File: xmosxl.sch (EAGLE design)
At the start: 139 parts, among them IC1 74LVC1T45W6-7, IC2 74LVC1T45W6-7, IC3 74LVC1T45W6-7, IC4 74LVC1T45W6-7, IC5 74LVC1T45W6-7, IC6 74ALVC164245DGG_11, IC7 74ALVC164245DGG_11, IC8 74LVC1T45W6-7, IC9 74LVC1T45W6-7, U1 24 MHz Osc. (F535L-24)

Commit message: Dd the link resistors
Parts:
- added R31, R32, R33, R34, R35: 33R, rcl:R-EU_R0201
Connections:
- new net N$27: R31.1, XMOS-LINK.X1D66@N2
- new net N$28: R32.1, XMOS-LINK.X1D67@P2
- new net N$29: R34.1, XMOS-LINK.X1D69@R1
- new net N$30: R35.1, XMOS-LINK.X1D70@R2
- net +5V: no longer JP1.13
- net RX0: no longer JP1.5
- net RX1: now also JP1.5; no longer JP1.9
- net RX2: now also JP1.9
- net RX3: now also JP1.13
- net RX4: now also R33.1
- net TX0: now also R31.2
- net TX1: now also R32.2
- net TX2: now also R33.2
- net TX3: now also R34.2
- net TX4: now also R35.2
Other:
- note removed: "Need to fix the RX lines, add 33R to tx, and place on grid"
- moved on the sheet: JP1

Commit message: Board circuit-complete. Decided to ditch the SPI expansion.
Need to set signal classes and routing hints
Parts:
- added JP2: (no value), pinhead:PINHD-2X9
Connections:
- new net XPND_CTRL0: JP2.3, XMOS-EXPAND.X3D00@D19
- new net XPND_CTRL1: JP2.5, XMOS-EXPAND.X3D01@D20
- new net XPND_CTRL2: JP2.7, XMOS-EXPAND.X3D10@C13
- new net XPND_CTRL3: JP2.9, XMOS-EXPAND.X3D11@D13
- new net XPND_CTRL4: JP2.11, XMOS-EXPAND.X3D12@AA12
- new net XPND_CTRL5: JP2.13, XMOS-EXPAND.X3D13@Y15
- new net XPND_CTRL6: JP2.15, XMOS-EXPAND.X3D24@Y19
- new net XPND_DATA0: JP2.2, XMOS-EXPAND.X3D02@U21
- new net XPND_DATA1: JP2.4, XMOS-EXPAND.X3D03@T21
- new net XPND_DATA2: JP2.6, XMOS-EXPAND.X3D04@R20
- new net XPND_DATA3: JP2.8, XMOS-EXPAND.X3D05@R21
- new net XPND_DATA4: JP2.10, XMOS-EXPAND.X3D06@P20
- new net XPND_DATA5: JP2.12, XMOS-EXPAND.X3D07@P21
- new net XPND_DATA6: JP2.14, XMOS-EXPAND.X3D08@E20
- new net XPND_DATA7: JP2.16, XMOS-EXPAND.X3D09@E21
- net +3V3: now also SLOT1.B16, SLOT2.B17, SLOT3.B16, SLOT3.B17, SLOT4.B18, SLOT5.B16, SLOT5.B18; no longer JP1.11, JP1.12
- net +5V: now also JP1.3, JP1.4, JP2.1, SLOT1.A1, SLOT1.A2, SLOT1.B1, SLOT1.B2, SLOT2.A1, SLOT2.A2, SLOT2.B1, SLOT2.B2, SLOT3.A1, SLOT3.A2, SLOT3.B1, SLOT3.B2, SLOT4.A1, SLOT4.A2, SLOT4.B1, SLOT4.B2, SLOT5.A1, SLOT5.A2, SLOT5.B1, SLOT5.B2
- net GND: now also JP1.11, JP1.12, JP1.15, JP1.16, JP2.17, JP2.18, SLOT1.B17, SLOT1.B18, SLOT1.B19, SLOT1.B20, SLOT1.B21, SLOT1.B22, SLOT1.B23, SLOT1.B24, SLOT1.B25, SLOT1.B26, SLOT1.B27, SLOT1.B28, SLOT1.B29, SLOT1.B30, SLOT1.B31, SLOT1.B32, SLOT2.B16, SLOT2.B18, SLOT2.B19, SLOT2.B20, SLOT2.B21, SLOT2.B22, SLOT2.B23, SLOT2.B24, SLOT2.B25, SLOT2.B26, SLOT2.B27, SLOT2.B28, SLOT2.B29, SLOT2.B30, SLOT2.B31, SLOT2.B32, SLOT3.B18, SLOT3.B19, SLOT3.B20, SLOT3.B21, SLOT3.B22, SLOT3.B23, SLOT3.B24, SLOT3.B25, SLOT3.B26, SLOT3.B27, SLOT3.B28, SLOT3.B29, SLOT3.B30, SLOT3.B31, SLOT3.B32, SLOT4.B16, SLOT4.B17, SLOT4.B19, SLOT4.B20, SLOT4.B21, SLOT4.B22, SLOT4.B23, SLOT4.B24, SLOT4.B25, SLOT4.B26, SLOT4.B27, SLOT4.B28, SLOT4.B29, SLOT4.B30, SLOT4.B31, SLOT4.B32, SLOT5.B17, SLOT5.B19, SLOT5.B20, SLOT5.B21, SLOT5.B22, SLOT5.B23, SLOT5.B24, SLOT5.B25, SLOT5.B26, SLOT5.B27, SLOT5.B28, SLOT5.B29, SLOT5.B30, SLOT5.B31, SLOT5.B32; no longer JP1.3, JP1.4
- net SBUS_A0: now also SLOT1.A3, SLOT2.A3, SLOT3.A3, SLOT4.A3, SLOT5.A3
- net SBUS_A1: now also SLOT1.A4, SLOT2.A4, SLOT3.A4, SLOT4.A4, SLOT5.A4
- net SBUS_A10: now also SLOT1.A13, SLOT2.A13, SLOT3.A13, SLOT4.A13, SLOT5.A13
- net SBUS_A11: now also SLOT1.A14, SLOT2.A14, SLOT3.A14, SLOT4.A14, SLOT5.A14
- net SBUS_A12: now also SLOT1.A15, SLOT2.A15, SLOT3.A15, SLOT4.A15, SLOT5.A15
- net SBUS_A13: now also SLOT1.A16, SLOT2.A16, SLOT3.A16, SLOT4.A16, SLOT5.A16
- net SBUS_A14: now also SLOT1.A17, SLOT2.A17, SLOT3.A17, SLOT4.A17, SLOT5.A17
- net SBUS_A15: now also SLOT1.A18, SLOT2.A18, SLOT3.A18, SLOT4.A18, SLOT5.A18
- net SBUS_A2: now also SLOT1.A5, SLOT2.A5, SLOT3.A5, SLOT4.A5, SLOT5.A5
- net SBUS_A3: now also SLOT1.A6, SLOT2.A6, SLOT3.A6, SLOT4.A6, SLOT5.A6
- net SBUS_A4: now also SLOT1.A7, SLOT2.A7, SLOT3.A7, SLOT4.A7, SLOT5.A7
- net SBUS_A5: now also SLOT1.A8, SLOT2.A8, SLOT3.A8, SLOT4.A8, SLOT5.A8
- net SBUS_A6: now also SLOT1.A9, SLOT2.A9, SLOT3.A9, SLOT4.A9, SLOT5.A9
- net SBUS_A7: now also SLOT1.A10, SLOT2.A10, SLOT3.A10, SLOT4.A10, SLOT5.A10
- net SBUS_A8: now also SLOT1.A11, SLOT2.A11, SLOT3.A11, SLOT4.A11, SLOT5.A11
- net SBUS_A9: now also SLOT1.A12, SLOT2.A12, SLOT3.A12, SLOT4.A12, SLOT5.A12
- net SBUS_CLK: now also SLOT1.A19, SLOT2.A19, SLOT3.A19, SLOT4.A19, SLOT5.A19
- net SBUS_D0: now also SLOT1.A20, SLOT2.A20, SLOT3.A20, SLOT4.A20, SLOT5.A20
- net SBUS_D1: now also SLOT1.A21, SLOT2.A21, SLOT3.A21, SLOT4.A21, SLOT5.A21
- net SBUS_D2: now also SLOT1.A22, SLOT2.A22, SLOT3.A22, SLOT4.A22, SLOT5.A22
- net SBUS_D3: now also SLOT1.A23, SLOT2.A23, SLOT3.A23, SLOT4.A23, SLOT5.A23
- net SBUS_D4: now also SLOT1.A24, SLOT2.A24, SLOT3.A24, SLOT4.A24, SLOT5.A24
- net SBUS_D5: now also SLOT1.A25, SLOT2.A25, SLOT3.A25, SLOT4.A25, SLOT5.A25
- net SBUS_D6: now also SLOT1.A26, SLOT2.A26, SLOT3.A26, SLOT4.A26, SLOT5.A26
- net SBUS_D7: now also SLOT1.A27, SLOT2.A27, SLOT3.A27, SLOT4.A27, SLOT5.A27
- net SBUS_FLG0: now also SLOT1.A28, SLOT2.A28, SLOT3.A28, SLOT4.A28, SLOT5.A28
- net SBUS_FLG1: now also SLOT1.A29, SLOT2.A29, SLOT3.A29, SLOT4.A29, SLOT5.A29
- net SBUS_FLG2: now also SLOT1.A30, SLOT2.A30, SLOT3.A30, SLOT4.A30, SLOT5.A30
- net SBUS_FLG3: now also SLOT1.A31, SLOT2.A31, SLOT3.A31, SLOT4.A31, SLOT5.A31
- net SBUS_FLG4: now also SLOT1.A32, SLOT2.A32, SLOT3.A32, SLOT4.A32, SLOT5.A32
- net SPI_BOPT0: now also SLOT1.B3, SLOT2.B3, SLOT3.B3, SLOT4.B3, SLOT5.B3
- net SPI_BOPT1: now also SLOT1.B4, SLOT2.B4, SLOT3.B4, SLOT4.B4, SLOT5.B4
- net SPI_BOPT2: now also SLOT1.B5, SLOT2.B5, SLOT3.B5, SLOT4.B5, SLOT5.B5
- net SPI_BOPT3: now also SLOT1.B6, SLOT2.B6, SLOT3.B6, SLOT4.B6, SLOT5.B6
- net SPI_BSEL0: now also SLOT1.B7, SLOT2.B7, SLOT3.B7, SLOT4.B7, SLOT5.B7
- net SPI_BSEL1: now also SLOT1.B8, SLOT2.B8, SLOT3.B8, SLOT4.B8, SLOT5.B8
- net SPI_BSEL2: now also SLOT1.B9, SLOT2.B9, SLOT3.B9, SLOT4.B9, SLOT5.B9
- net SPI_BSEL3: now also SLOT1.B10, SLOT2.B10, SLOT3.B10, SLOT4.B10, SLOT5.B10
- net SPI_CLK0: now also SLOT1.B11, SLOT2.B11, SLOT3.B11, SLOT4.B11, SLOT5.B11
- net SPI_IRQ0: now also SLOT1.B12
- net SPI_IRQ1: now also SLOT2.B12
- net SPI_IRQ2: now also SLOT3.B12
- net SPI_IRQ3: now also SLOT4.B12
- net SPI_IRQ4: now also SLOT5.B12
- net SPI_MISO0: now also SLOT1.B13, SLOT2.B13, SLOT3.B13, SLOT4.B13, SLOT5.B13
- net SPI_MOSI0: now also SLOT1.B14, SLOT2.B14, SLOT3.B14, SLOT4.B14, SLOT5.B14
- net SPI_SS0: now also SLOT1.B15
- net SPI_SS1: now also SLOT2.B15
- net SPI_SS2: now also SLOT3.B15
- net SPI_SS3: now also SLOT4.B15
- net SPI_SS4: now also SLOT5.B15
- net VDD: no longer JP1.15, JP1.16
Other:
- moved on the sheet: SLOT1, SLOT2, SLOT3

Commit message: Start reconfiguring for STM
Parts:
- removed C10, C11, C14, C21, C22, C23, C24, C25, C26, C27, C28, C29, C30, C31, C32, C33, C34, C35, C36, C37, C38, C39, C4, C40, C43, C54, C55, C58, C7, C8, C9: 0.1uF, rcl:C-EUC0201
- removed C41, C42, C47: 10uF, rcl:C-EUC0402K
- removed C46, C48: 1uF, rcl:C-EUC0402K
- removed C49: 0.1uF, rcl:C-EUC0402
- removed C50: 120pF, rcl:C-EUC0402
- removed C56: 120pF, rcl:C-EUC0201
- removed C57: 10nF, rcl:C-EUC0201
- removed C59, C60, C61, C62, C63, C64, C65, C66: 100nF, rcl:C-EUC0201
- removed I2C0, I2C1: (no value), pinhead:PINHD-1X2
- removed IC2, IC3, IC4, IC5: 74LVC1T45W6-7, samacsys:74LVC1T45W6-7
- removed JP2: (no value), pinhead:PINHD-2X9
- removed JTAG5V: PSU, pinhead:PINHD-1X2
- removed NOR: SN74LVC1G02, sjg-logic:SN74LVC1G02
- removed R1, R12, R13, R18, R19, R2, R22, R23, R25, R26, R3, R5, R6, R7, R9: 10K, rcl:R-EU_R0201
- removed R10: 47K, rcl:R-EU_R0402
- removed R14, R15: 47K, rcl:R-EU_R0201
- removed R16, R17, R31, R32, R33, R34, R35: 33R, rcl:R-EU_R0201
- removed R24: 2.2R, rcl:R-EU_R0201
- removed R27, R28: 43R2, rcl:R-EU_R0201
- removed R29, R30: 4K7, rcl:R-EU_R0201
- removed RESET_SW: MANUAL_RESET, SparkFun:TAC_SWITCHPTH
- removed U$11: TPS3808G09DBVR, sjg-power:TPS3808G09DBVR
- removed U$3: LD49300, sjg-power:LD49150
- removed U$4: TPS3808G33DBVR, sjg-power:TPS3808DBVR
- removed U$5: 74LVC1G07SE-7, sjg-logic:74LVC1G07SE-7
- removed U$7: W9852G6KH, sjg-sdram:W9852G6KH
- removed UART: (no value), pinhead:PINHD-1X3
- removed XMOS: XEF232, xmosxl:XEF232
- removed XTAG: 1175-1618-ND, pinhead:PINHD-2X10/90
- added SLOT6: PCIE_64, pcie:PCIE_64
- added U$1: STM32F767, xmosxl:STM32F767
- C1, C2: value 0.1uF -> 10uF; device rcl:C-EUC0201 -> rcl:C-EUC0402K; USE GRM033C80J104ME15D -> (none)
- C3: value 0.1uF -> 1uF
- IC1: value 74LVC1T45W6-7 -> MCP1727-1802E_SN; device samacsys:74LVC1T45W6-7 -> samacsys:MCP1727-1802E_SN
- JP1: device pinhead:PINHD-2X9 -> pinhead:PINHD-2X20
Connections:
- removed net !DEBUG!: XMOS-CTRL.!DEBUG!@D9, XTAG.11
- removed net !HALT!_DIR: IC4.DIR, R7.1, XMOS-A8BUS.X3D29@C14
- removed net !IRQ!: IC3.B, XMOS-A8BUS.X2D35@B21
- removed net !IRQ!_DIR: IC3.DIR, R6.1, XMOS-A8BUS.X3D28@D14
- removed net !REF!_DIR: IC8.DIR, R9.1, XMOS-A8BUS.X3D30@A15
- removed net !RESET!: R15.1, U$11.!RESET!@1, U$5.Y@4, XMOS-CTRL.!RST!@B12, XMOS-CTRL.!TRST!@C12
- removed net !RST!_DIR: IC2.DIR, R5.1, XMOS-A8BUS.X3D27@B16
- removed net !SD_CAS!: NORG$1.I0, U$7.!CAS!@17, XMOS-SDRAM.X2D20@Y18
- removed net !SD_RAS!: U$7.!RAS!@18, XMOS-SDRAM.X2D02@Y13
- removed net !SD_WE!: NORG$1.I1, U$7.!WE!@16, XMOS-SDRAM.X2D21@AA18
- removed net A_DIR: IC7.1DIR, IC7.2DIR, R2.1, XMOS-A8BUS.X3D31@B15
- removed net D_DIR: IC6.1DIR, R3.1, XMOS-A8BUS.X3D32@A14
- removed net EN_1V0: R10.1, U$3.EN, U$4.!RESET!@1
- removed net JTAG_DN0: XMOS-LINK.X1D17@U1, XTAG.14
- removed net JTAG_DN1: XMOS-LINK.X1D16@U2, XTAG.18
- removed net JTAG_UP0: R16.2, XTAG.10
- removed net JTAG_UP1: R17.2, XTAG.6
- removed net N$1: R14.1, U$5.A@2, XTAG.15
- removed net N$10: R26.2, XMOS-CTRL.MODE0@D10
- removed net N$11: R27.2, XMOS-USB.USB_RTUNE_1@W16
- removed net N$12: R28.2, XMOS-USB.USB_RTUNE_0@W6
- removed net N$13: UART.2, XMOS-UART.X1D35@E3
- removed net N$14: NORG$1.O, U$7.LDQM@15, U$7.UDQM@39
- removed net N$15: R12.2, U$7.CKE@37
- removed net N$17: R13.2, U$7.!CS!@19
- removed net N$20: UART.1, XMOS-UART.X1D34@D3
- removed net N$22: R16.1, XMOS-LINK.X1D18@V2
- removed net N$23: R17.1, XMOS-LINK.X1D19@V1
- removed net N$27: R31.1, XMOS-LINK.X1D66@N2
- removed net N$28: R32.1, XMOS-LINK.X1D67@P2
- removed net N$29: R34.1, XMOS-LINK.X1D69@R1
- removed net N$30: R35.1, XMOS-LINK.X1D70@R2
- removed net N$38: JTAG5V.2, XTAG.1
- removed net N$5: C50.1, U$4.CT@4
- removed net N$6: C56.1, U$11.CT@4
- removed net N$7: C58.1, R24.2, XMOS-POWER.PLL_AVDD@F11
- removed net N$8: R14.2, U$5.VCC@5
- removed net N$9: R25.1, XMOS-CTRL.MODE1@C10
- removed net R/!W!_DIR: IC1.DIR, R1.1, XMOS-A8BUS.X3D26@D15
- removed net RD4: IC6.2A1, XMOS-A8BUS.X3D20@W18
- removed net RD5: IC6.2A0, XMOS-A8BUS.X3D21@V18
- removed net RX0: JP1.1, XMOS-LINK.X1D65@N1
- removed net RX1: JP1.5, XMOS-LINK.X1D64@M1
- removed net RX2: JP1.9, XMOS-LINK.X1D63@M2
- removed net RX3: JP1.13, XMOS-LINK.X1D62@M3
- removed net RX4: JP1.17, R33.1, XMOS-LINK.X1D61@L3, XMOS-LINK.X1D68@P1
- removed net SBUS_A0: SLOT1.A3, SLOT2.A3, SLOT3.A3, SLOT4.A3, SLOT5.A3, XMOS-SLOTBUS.X1D26@A5
- removed net SBUS_A1: SLOT1.A4, SLOT2.A4, SLOT3.A4, SLOT4.A4, SLOT5.A4, XMOS-SLOTBUS.X1D27@B5
- removed net SBUS_A10: SLOT1.A13, SLOT2.A13, SLOT3.A13, SLOT4.A13, SLOT5.A13, XMOS-SLOTBUS.X1D38@T1
- removed net SBUS_A11: SLOT1.A14, SLOT2.A14, SLOT3.A14, SLOT4.A14, SLOT5.A14, XMOS-SLOTBUS.X1D39@U3
- removed net SBUS_A12: SLOT1.A15, SLOT2.A15, SLOT3.A15, SLOT4.A15, SLOT5.A15, XMOS-SLOTBUS.X1D40@B7
- removed net SBUS_A13: SLOT1.A16, SLOT2.A16, SLOT3.A16, SLOT4.A16, SLOT5.A16, XMOS-SLOTBUS.X1D41@A7
- removed net SBUS_A14: SLOT1.A17, SLOT2.A17, SLOT3.A17, SLOT4.A17, SLOT5.A17, XMOS-SLOTBUS.X1D42@B6
- removed net SBUS_A15: SLOT1.A18, SLOT2.A18, SLOT3.A18, SLOT4.A18, SLOT5.A18, XMOS-SLOTBUS.X1D43@C6
- removed net SBUS_A2: SLOT1.A5, SLOT2.A5, SLOT3.A5, SLOT4.A5, SLOT5.A5, XMOS-SLOTBUS.X1D28@C5
- removed net SBUS_A3: SLOT1.A6, SLOT2.A6, SLOT3.A6, SLOT4.A6, SLOT5.A6, XMOS-SLOTBUS.X1D29@D5
- removed net SBUS_A4: SLOT1.A7, SLOT2.A7, SLOT3.A7, SLOT4.A7, SLOT5.A7, XMOS-SLOTBUS.X1D30@C4
- removed net SBUS_A5: SLOT1.A8, SLOT2.A8, SLOT3.A8, SLOT4.A8, SLOT5.A8, XMOS-SLOTBUS.X1D31@D4
- removed net SBUS_A6: SLOT1.A9, SLOT2.A9, SLOT3.A9, SLOT4.A9, SLOT5.A9, XMOS-SLOTBUS.X1D32@A4
- removed net SBUS_A7: SLOT1.A10, SLOT2.A10, SLOT3.A10, SLOT4.A10, SLOT5.A10, XMOS-SLOTBUS.X1D33@B4
- removed net SBUS_A8: SLOT1.A11, SLOT2.A11, SLOT3.A11, SLOT4.A11, SLOT5.A11, XMOS-SLOTBUS.X1D36@F1
- removed net SBUS_A9: SLOT1.A12, SLOT2.A12, SLOT3.A12, SLOT4.A12, SLOT5.A12, XMOS-SLOTBUS.X1D37@R3
- removed net SBUS_CLK: SLOT1.A19, SLOT2.A19, SLOT3.A19, SLOT4.A19, SLOT5.A19, XMOS-SLOTBUS.X1D21@AA8
- removed net SBUS_D0: SLOT1.A20, SLOT2.A20, SLOT3.A20, SLOT4.A20, SLOT5.A20, XMOS-SLOTBUS.X1D49@G1
- removed net SBUS_D1: SLOT1.A21, SLOT2.A21, SLOT3.A21, SLOT4.A21, SLOT5.A21, XMOS-SLOTBUS.X1D50@G2
- removed net SBUS_D2: SLOT1.A22, SLOT2.A22, SLOT3.A22, SLOT4.A22, SLOT5.A22, XMOS-SLOTBUS.X1D51@G3
- removed net SBUS_D3: SLOT1.A23, SLOT2.A23, SLOT3.A23, SLOT4.A23, SLOT5.A23, XMOS-SLOTBUS.X1D52@H2
- removed net SBUS_D4: SLOT1.A24, SLOT2.A24, SLOT3.A24, SLOT4.A24, SLOT5.A24, XMOS-SLOTBUS.X1D53@H1
- removed net SBUS_D5: SLOT1.A25, SLOT2.A25, SLOT3.A25, SLOT4.A25, SLOT5.A25, XMOS-SLOTBUS.X1D54@J1
- removed net SBUS_D6: SLOT1.A26, SLOT2.A26, SLOT3.A26, SLOT4.A26, SLOT5.A26, XMOS-SLOTBUS.X1D55@J2
- removed net SBUS_D7: SLOT1.A27, SLOT2.A27, SLOT3.A27, SLOT4.A27, SLOT5.A27, XMOS-SLOTBUS.X1D56@K3
- removed net SBUS_FLG0: SLOT1.A28, SLOT2.A28, SLOT3.A28, SLOT4.A28, SLOT5.A28, XMOS-SLOTBUS.X1D57@K2
- removed net SBUS_FLG1: SLOT1.A29, SLOT2.A29, SLOT3.A29, SLOT4.A29, SLOT5.A29, XMOS-SLOTBUS.X1D58@K1
- removed net SBUS_FLG2: SLOT1.A30, SLOT2.A30, SLOT3.A30, SLOT4.A30, SLOT5.A30, XMOS-SLOTBUS.X1D14@V8
- removed net SBUS_FLG3: SLOT1.A31, SLOT2.A31, SLOT3.A31, SLOT4.A31, SLOT5.A31, XMOS-SLOTBUS.X1D15@W8
- removed net SBUS_FLG4: SLOT1.A32, SLOT2.A32, SLOT3.A32, SLOT4.A32, SLOT5.A32, XMOS-SLOTBUS.X1D20@Y8
- removed net SCL: I2C0.1, I2C1.1, R29.1, XMOS-I2C.X1D11@A3
- removed net SDA: I2C0.2, I2C1.2, R30.1, XMOS-I2C.X1D10@B3
- removed net SD_ADQ0: U$7.A0@23, U$7.DQ0@2, XMOS-SDRAM.X2D03@AA13
- removed net SD_ADQ1: R19.2, U$7.A1@24, U$7.DQ1@4, XMOS-SDRAM.X2D04@W13
- removed net SD_ADQ10: U$7.A10/AP@22, U$7.DQ10@45, XMOS-SDRAM.X2D14@Y17
- removed net SD_ADQ11: U$7.A11@35, U$7.DQ11@47, XMOS-SDRAM.X2D15@AA17
- removed net SD_ADQ12: U$7.A12@36, U$7.DQ12@48, XMOS-SDRAM.X2D16@W21
- removed net SD_ADQ13: U$7.BS0@20, U$7.DQ13@50, XMOS-SDRAM.X2D17@V20
- removed net SD_ADQ14: U$7.BS1@21, U$7.DQ14@51, XMOS-SDRAM.X2D18@V21
- removed net SD_ADQ15: U$7.DQ15@53, XMOS-SDRAM.X2D19@U20
- removed net SD_ADQ2: R22.2, U$7.A2@25, U$7.DQ2@5, XMOS-SDRAM.X2D05@V13
- removed net SD_ADQ3: R18.2, U$7.A3@26, U$7.DQ3@7, XMOS-SDRAM.X2D06@W14
- removed net SD_ADQ4: U$7.A4@29, U$7.DQ4@8, XMOS-SDRAM.X2D07@V14
- removed net SD_ADQ5: U$7.A5@30, U$7.DQ5@10, XMOS-SDRAM.X2D08@Y14
- removed net SD_ADQ6: U$7.A6@31, U$7.DQ6@11, XMOS-SDRAM.X2D09@AA14
- removed net SD_ADQ7: R23.2, U$7.A7@32, U$7.DQ7@13, XMOS-SDRAM.X2D11@Y12
- removed net SD_ADQ8: U$7.A8@33, U$7.DQ8@42, XMOS-SDRAM.X2D12@V19
- removed net SD_ADQ9: U$7.A9@34, U$7.DQ9@44, XMOS-SDRAM.X2D13@Y20
- removed net SD_CLK: U$7.CLK@38, XMOS-SDRAM.X2D00@W12
- removed net SPI_BOPT0: SLOT1.B3, SLOT2.B3, SLOT3.B3, SLOT4.B3, SLOT5.B3, XMOS-SPI.X0D14@W9
- removed net SPI_BOPT1: SLOT1.B4, SLOT2.B4, SLOT3.B4, SLOT4.B4, SLOT5.B4, XMOS-SPI.X0D15@Y9
- removed net SPI_BOPT2: SLOT1.B5, SLOT2.B5, SLOT3.B5, SLOT4.B5, SLOT5.B5, XMOS-SPI.X0D20@AA9
- removed net SPI_BOPT3: SLOT1.B6, SLOT2.B6, SLOT3.B6, SLOT4.B6, SLOT5.B6, XMOS-SPI.X0D21@V10
- removed net SPI_BSEL0: SLOT1.B7, SLOT2.B7, SLOT3.B7, SLOT4.B7, SLOT5.B7, XMOS-SPI.X0D02@V4
- removed net SPI_BSEL1: SLOT1.B8, SLOT2.B8, SLOT3.B8, SLOT4.B8, SLOT5.B8, XMOS-SPI.X0D03@W4
- removed net SPI_BSEL2: SLOT1.B9, SLOT2.B9, SLOT3.B9, SLOT4.B9, SLOT5.B9, XMOS-SPI.X0D08@V5
- removed net SPI_BSEL3: SLOT1.B10, SLOT2.B10, SLOT3.B10, SLOT4.B10, SLOT5.B10, XMOS-SPI.X0D09@W5
- removed net SPI_CLK0: SLOT1.B11, SLOT2.B11, SLOT3.B11, SLOT4.B11, SLOT5.B11, XMOS-SPI.X0D00@Y2
- removed net SPI_CLK1: XMOS-SPI.X1D22@W2
- removed net SPI_IRQ0: SLOT1.B12, XMOS-SPI.X0D28@B9
- removed net SPI_IRQ1: SLOT2.B12, XMOS-SPI.X0D29@A9
- removed net SPI_IRQ2: SLOT3.B12, XMOS-SPI.X0D30@B8
- removed net SPI_IRQ3: SLOT4.B12, XMOS-SPI.X0D31@A8
- removed net SPI_IRQ4: SLOT5.B12, XMOS-SPI.X0D32@C9
- removed net SPI_IRQ5: XMOS-SPI.X0D33@C8
- removed net SPI_IRQ6: XMOS-SPI.X0D40@D2
- removed net SPI_IRQ7: XMOS-SPI.X0D41@D1
- removed net SPI_IRQ8: XMOS-SPI.X0D42@E2
- removed net SPI_IRQ9: XMOS-SPI.X0D43@E1
- removed net SPI_MISO0: SLOT1.B13, SLOT2.B13, SLOT3.B13, SLOT4.B13, SLOT5.B13, XMOS-SPI.X0D11@V6
- removed net SPI_MISO1: XMOS-SPI.X1D23@Y1
- removed net SPI_MOSI0: SLOT1.B14, SLOT2.B14, SLOT3.B14, SLOT4.B14, SLOT5.B14, XMOS-SPI.X0D12@W10
- removed net SPI_MOSI1: XMOS-SPI.X1D24@Y7
- removed net SPI_SS0: SLOT1.B15, XMOS-SPI.X0D13@Y10
- removed net SPI_SS1: SLOT2.B15, XMOS-SPI.X0D22@AA10
- removed net SPI_SS2: SLOT3.B15, XMOS-SPI.X0D23@W11
- removed net SPI_SS3: SLOT4.B15, XMOS-SPI.X0D36@B2
- removed net SPI_SS4: SLOT5.B15, XMOS-SPI.X0D37@B1
- removed net SPI_SS5: XMOS-SPI.X0D38@C2
- removed net SPI_SS6: XMOS-SPI.X0D39@C1
- removed net SPI_SS7: XMOS-SPI.X1D12@Y5
- removed net SPI_SS8: XMOS-SPI.X1D13@AA5
- removed net SPI_SS9: XMOS-SPI.X1D25@V9
- removed net TCK: XMOS-CTRL.TCK@B13, XTAG.9
- removed net TDI: XMOS-CTRL.TDI@A10, XTAG.5
- removed net TDO: XMOS-CTRL.TDO@A13, XTAG.13
- removed net TMS: XMOS-CTRL.TMS@D12, XTAG.7
- removed net TRST_N: C57.2, RESET_SW.1, RESET_SW.2, U$11.!MR!@3
- removed net TX0: JP1.2, R31.2
- removed net TX1: JP1.6, R32.2
- removed net TX2: JP1.10, R33.2
- removed net TX3: JP1.14, R34.2
- removed net TX4: JP1.18, R35.2
- removed net UART_RX: XTAG.19
- removed net UART_TX: XTAG.17
- removed net VDD: C29.1, C30.1, C31.1, C32.1, C33.1, C34.1, C35.1, C36.1, C37.1, C38.1, C39.1, C40.1, C42.1, C47.1, R24.1, U$11.SENSE@5, U$3.VOUT, XMOS-POWER.VDD@C19, XMOS-POWER.VDD@C3, XMOS-POWER.VDD@E13, XMOS-POWER.VDD@E14, XMOS-POWER.VDD@E17, XMOS-POWER.VDD@E18, XMOS-POWER.VDD@E4, XMOS-POWER.VDD@E5, XMOS-POWER.VDD@E8, XMOS-POWER.VDD@E9, XMOS-POWER.VDD@F12, XMOS-POWER.VDD@F13, XMOS-POWER.VDD@F14, XMOS-POWER.VDD@F15, XMOS-POWER.VDD@F16, XMOS-POWER.VDD@F17, XMOS-POWER.VDD@F18, XMOS-POWER.VDD@F4, XMOS-POWER.VDD@F5, XMOS-POWER.VDD@F6, XMOS-POWER.VDD@F7, XMOS-POWER.VDD@F8, XMOS-POWER.VDD@F9, XMOS-POWER.VDD@H19, XMOS-POWER.VDD@H3, XMOS-POWER.VDD@J19, XMOS-POWER.VDD@J3, XMOS-POWER.VDD@N19, XMOS-POWER.VDD@N3, XMOS-POWER.VDD@P19, XMOS-POWER.VDD@P3, XMOS-POWER.VDD@T10, XMOS-POWER.VDD@T12, XMOS-POWER.VDD@T13, XMOS-POWER.VDD@T14, XMOS-POWER.VDD@T16, XMOS-POWER.VDD@T17, XMOS-POWER.VDD@T18, XMOS-POWER.VDD@T4, XMOS-POWER.VDD@T5, XMOS-POWER.VDD@T6, XMOS-POWER.VDD@T8, XMOS-POWER.VDD@T9, XMOS-POWER.VDD@U13, XMOS-POWER.VDD@U14, XMOS-POWER.VDD@U17, XMOS-POWER.VDD@U18, XMOS-POWER.VDD@U4, XMOS-POWER.VDD@U5, XMOS-POWER.VDD@U9
- removed net XPND_CTRL0: JP2.3, XMOS-EXPAND.X3D00@D19
- removed net XPND_CTRL1: JP2.5, XMOS-EXPAND.X3D01@D20
- removed net XPND_CTRL2: JP2.7, XMOS-EXPAND.X3D10@C13
- removed net XPND_CTRL3: JP2.9, XMOS-EXPAND.X3D11@D13
- removed net XPND_CTRL4: JP2.11, XMOS-EXPAND.X3D12@AA12
- removed net XPND_CTRL5: JP2.13, XMOS-EXPAND.X3D13@Y15
- removed net XPND_CTRL6: JP2.15, XMOS-EXPAND.X3D24@Y19
- removed net XPND_DATA0: JP2.2, XMOS-EXPAND.X3D02@U21
- removed net XPND_DATA1: JP2.4, XMOS-EXPAND.X3D03@T21
- removed net XPND_DATA2: JP2.6, XMOS-EXPAND.X3D04@R20
- removed net XPND_DATA3: JP2.8, XMOS-EXPAND.X3D05@R21
- removed net XPND_DATA4: JP2.10, XMOS-EXPAND.X3D06@P20
- removed net XPND_DATA5: JP2.12, XMOS-EXPAND.X3D07@P21
- removed net XPND_DATA6: JP2.14, XMOS-EXPAND.X3D08@E20
- removed net XPND_DATA7: JP2.16, XMOS-EXPAND.X3D09@E21
- new net +1.2V: C2.1, C3.1, IC1.SENSE, IC1.VOUT
- new net N$33: C53.1, U1.GND
- net !EXTSEL!: no longer XMOS-A8BUS.X2D24@D21
- net !EXTSEL!_DIR: no longer XMOS-A8BUS.X3D33@B14
- net !HALT!: now also IC6.2A3; no longer IC4.B, XMOS-A8BUS.X2D36@B10
- net !HI_EXTSEL!: now also U$1-A8.PC2@37
- net !HI_HALT!: now also IC6.2B3, U$1-A8.PC6@138; no longer IC4.A
- net !HI_IRQ!: now also U$1-A8.PC5@58; no longer IC3.A
- net !HI_MPD!: now also IC8.A, U$1-A8.PC3@38; no longer IC5.A
- net !HI_REF!: now also IC6.2B0, U$1-A8.PC7@139; no longer IC8.A
- net !HI_RST!: now also IC6.2B4, U$1-A8.PC4@57; no longer IC2.A
- net !MPD!: now also IC8.B; no longer IC5.B, XMOS-A8BUS.X2D25@C20
- net !MPD!_DIR: now also IC8.DIR; no longer IC5.DIR, XMOS-A8BUS.X3D25@AA19
- net !REF!: now also IC6.2A0; no longer IC8.B, XMOS-A8BUS.X3D23@V12
- net !RST!: now also IC6.2A4; no longer IC2.B, XMOS-A8BUS.X2D34@C21
- net +3V3: no longer C10.1, C14.1, C21.1, C22.1, C23.1, C24.1, C25.1, C26.1, C27.1, C28.1, C41.1, C43.1, C49.1, C54.1, C55.1, C59.1, C60.1, C61.1, C62.1, C63.1, C64.1, C65.1, C66.1, C7.1, C8.1, C9.1, IC1.VCC(B), IC2.VCC(B), IC3.VCC(B), IC4.VCC(B), IC5.VCC(B), NORG$2.VCC, R1.2, R10.2, R11.1, R12.1, R15.2, R18.1, R25.2, R29.2, R30.2, R5.2, R6.2, R7.2, R8.2, R9.2, SLOT1.B16, SLOT2.B17, SLOT3.B16, SLOT3.B17, SLOT4.B18, SLOT5.B16, SLOT5.B18, U$11.VDD@6, U$4.SENSE@5, U$4.VDD@6, U$7.VDD@1, U$7.VDD@14, U$7.VDD@27, U$7.VDDQ@3, U$7.VDDQ@43, U$7.VDDQ@49, U$7.VDDQ@9, XMOS-POWER.OTP_VCC@C11, XMOS-POWER.VDDIO@A11, XMOS-POWER.VDDIO@A2, XMOS-POWER.VDDIO@A20, XMOS-POWER.VDDIO@AA11, XMOS-POWER.VDDIO@AA2, XMOS-POWER.VDDIO@AA20, XMOS-POWER.VDDIO@D7, XMOS-POWER.VDDIO@E15, XMOS-POWER.VDDIO@E7, XMOS-POWER.VDDIO@F2, XMOS-POWER.VDDIO@F20, XMOS-POWER.VDDIO@L1, XMOS-POWER.VDDIO@L21, XMOS-POWER.VDDIO@T2, XMOS-POWER.VDDIO@T20, XMOS-POWER.VDDIO@U11, XMOS-POWER.VDDIO@U15, XMOS-POWER.VDDIO@U7, XMOS-POWER.VDDIOT@A16, XMOS-POWER.VDDIOT@A6
- net +5V: now also IC1.!SHDN, IC1.VIN, IC1.VIN_1, SLOT6.A1, SLOT6.A2, SLOT6.B1, SLOT6.B2; no longer C11.1, C2.1, C3.1, C4.1, C46.1, C48.1, IC1.VCC(A), IC2.VCC(A), IC3.VCC(A), IC4.VCC(A), IC5.VCC(A), JP1.3, JP1.4, JP1.7, JP1.8, JP2.1, JTAG5V.1, U$3.VBIAS, U$3.VIN
- net A0: no longer XMOS-A8BUS.X2D49@R19
- net A1: no longer XMOS-A8BUS.X2D50@N20
- net A10: no longer XMOS-A8BUS.X2D61@J21
- net A11: no longer XMOS-A8BUS.X2D62@J20
- net A12: no longer XMOS-A8BUS.X2D63@H20
- net A13: no longer XMOS-A8BUS.X2D64@H21
- net A14: no longer XMOS-A8BUS.X2D65@G21
- net A15: no longer XMOS-A8BUS.X2D66@G20
- net A2: no longer XMOS-A8BUS.X2D51@N21
- net A3: no longer XMOS-A8BUS.X2D52@M21
- net A4: no longer XMOS-A8BUS.X2D53@M20
- net A5: no longer XMOS-A8BUS.X2D54@M19
- net A6: no longer XMOS-A8BUS.X2D55@L19
- net A7: no longer XMOS-A8BUS.X2D56@K19
- net A8: no longer XMOS-A8BUS.X2D57@K20
- net A9: no longer XMOS-A8BUS.X2D58@K21
- net CLK: no longer XMOS-A8BUS.X2D22@Y21
- net CTRL_DIR: now also IC6.1DIR, IC7.1DIR, IC7.2DIR
- net D0: no longer XMOS-A8BUS.X2D26@B20
- net D1: no longer XMOS-A8BUS.X2D27@B19
- net D2: no longer XMOS-A8BUS.X2D28@B18
- net D3: no longer XMOS-A8BUS.X2D29@A18
- net D4: no longer XMOS-A8BUS.X2D30@B17
- net D5: no longer XMOS-A8BUS.X2D31@A17
- net D6: no longer XMOS-A8BUS.X2D32@A19
- net D7: no longer XMOS-A8BUS.X2D33@C18
- net GND: now also R11.1, R8.2; no longer C10.2, C11.2, C14.2, C21.2, C22.2, C23.2, C24.2, C25.2, C26.2, C27.2, C28.2, C29.2, C30.2, C31.2, C32.2, C33.2, C34.2, C35.2, C36.2, C37.2, C38.2, C39.2, C4.2, C40.2, C41.2, C42.2, C43.2, C46.2, C47.2, C48.2, C49.2, C50.2, C53.1, C54.2, C55.2, C56.2, C57.1, C58.2, C59.2, C60.2, C61.2, C62.2, C63.2, C64.2, C65.2, C66.2, C7.2, C8.2, C9.2, IC2.GND, IC3.GND, IC4.GND, IC5.GND, IC6.2A3, IC6.2A4, IC6.2B3, IC6.2B4, JP1.11, JP1.12, JP1.15, JP1.16, JP2.17, JP2.18, NORG$2.GND, R13.1, R19.1, R2.2, R22.1, R23.1, R26.1, R27.1, R28.1, R3.2, RESET_SW.3, RESET_SW.4, SLOT1.B17, SLOT1.B18, SLOT1.B19, SLOT1.B20, SLOT1.B21, SLOT1.B22, SLOT1.B23, SLOT1.B24, SLOT1.B25, SLOT1.B26, SLOT1.B27, SLOT1.B28, SLOT1.B29, SLOT1.B30, SLOT1.B31, SLOT1.B32, SLOT2.B16, SLOT2.B18, SLOT2.B19, SLOT2.B20, SLOT2.B21, SLOT2.B22, SLOT2.B23, SLOT2.B24, SLOT2.B25, SLOT2.B26, SLOT2.B27, SLOT2.B28, SLOT2.B29, SLOT2.B30, SLOT2.B31, SLOT2.B32, SLOT3.B18, SLOT3.B19, SLOT3.B20, SLOT3.B21, SLOT3.B22, SLOT3.B23, SLOT3.B24, SLOT3.B25, SLOT3.B26, SLOT3.B27, SLOT3.B28, SLOT3.B29, SLOT3.B30, SLOT3.B31, SLOT3.B32, SLOT4.B16, SLOT4.B17, SLOT4.B19, SLOT4.B20, SLOT4.B21, SLOT4.B22, SLOT4.B23, SLOT4.B24, SLOT4.B25, SLOT4.B26, SLOT4.B27, SLOT4.B28, SLOT4.B29, SLOT4.B30, SLOT4.B31, SLOT4.B32, SLOT5.B17, SLOT5.B19, SLOT5.B20, SLOT5.B21, SLOT5.B22, SLOT5.B23, SLOT5.B24, SLOT5.B25, SLOT5.B26, SLOT5.B27, SLOT5.B28, SLOT5.B29, SLOT5.B30, SLOT5.B31, SLOT5.B32, U$11.GND@2, U$3.GND, U$4.GND@2, U$5.GND@3, U$7.VSS@28, U$7.VSS@41, U$7.VSS@54, U$7.VSSQ@12, U$7.VSSQ@46, U$7.VSSQ@52, U$7.VSSQ@6, U1.GND, UART.3, XMOS-A8BUS.X2D67@G19, XMOS-A8BUS.X2D68@F21, XMOS-A8BUS.X2D69@E19, XMOS-A8BUS.X2D70@D18, XMOS-A8BUS.X3D14@W17, XMOS-A8BUS.X3D15@V17, XMOS-POWER.GND@A1, XMOS-POWER.GND@A21, XMOS-POWER.GND@AA1, XMOS-POWER.GND@AA21, XMOS-POWER.GND@B11, XMOS-POWER.GND@C15, XMOS-POWER.GND@C7, XMOS-POWER.GND@D6, XMOS-POWER.GND@E16, XMOS-POWER.GND@E6, XMOS-POWER.GND@F19, XMOS-POWER.GND@F3, XMOS-POWER.GND@J13, XMOS-POWER.GND@J14, XMOS-POWER.GND@J15, XMOS-POWER.GND@J16, XMOS-POWER.GND@J17, XMOS-POWER.GND@J5, XMOS-POWER.GND@J6, XMOS-POWER.GND@J7, XMOS-POWER.GND@J8, XMOS-POWER.GND@J9, XMOS-POWER.GND@K13, XMOS-POWER.GND@K14, XMOS-POWER.GND@K15, XMOS-POWER.GND@K16, XMOS-POWER.GND@K17, XMOS-POWER.GND@K5, XMOS-POWER.GND@K6, XMOS-POWER.GND@K7, XMOS-POWER.GND@K8, XMOS-POWER.GND@K9, XMOS-POWER.GND@L13, XMOS-POWER.GND@L14, XMOS-POWER.GND@L15, XMOS-POWER.GND@L16, XMOS-POWER.GND@L17, XMOS-POWER.GND@L2, XMOS-POWER.GND@L20, XMOS-POWER.GND@L5, XMOS-POWER.GND@L6, XMOS-POWER.GND@L7, XMOS-POWER.GND@L8, XMOS-POWER.GND@L9, XMOS-POWER.GND@M13, XMOS-POWER.GND@M14, XMOS-POWER.GND@M15, XMOS-POWER.GND@M16, XMOS-POWER.GND@M17, XMOS-POWER.GND@M5, XMOS-POWER.GND@M6, XMOS-POWER.GND@M7, XMOS-POWER.GND@M8, XMOS-POWER.GND@M9, XMOS-POWER.GND@N13, XMOS-POWER.GND@N14, XMOS-POWER.GND@N15, XMOS-POWER.GND@N16, XMOS-POWER.GND@N17, XMOS-POWER.GND@N5, XMOS-POWER.GND@N6, XMOS-POWER.GND@N7, XMOS-POWER.GND@N8, XMOS-POWER.GND@N9, XMOS-POWER.GND@T11, XMOS-POWER.GND@T19, XMOS-POWER.GND@T3, XMOS-POWER.GND@U16, XMOS-POWER.GND@U6, XMOS-POWER.GND@W15, XMOS-POWER.GND@W7, XMOS-POWER.GND@Y11, XMOS-POWER.PLL_AGND@F10, XTAG.12, XTAG.16, XTAG.20, XTAG.4, XTAG.8
- net HI_A0: now also U$1-A8.PB0@61
- net HI_A1: now also U$1-A8.PB1@62
- net HI_A10: now also U$1-A8.PB10@90
- net HI_A11: now also U$1-A8.PB11@91
- net HI_A12: now also U$1-A8.PB12@104
- net HI_A13: now also U$1-A8.PB13@105
- net HI_A14: now also U$1-A8.PB14@106
- net HI_A15: now also U$1-A8.PB15@107
- net HI_A2: now also U$1-A8.PB2@63
- net HI_A3: now also U$1-A8.PB3@192
- net HI_A4: now also U$1-A8.PB4@193
- net HI_A5: now also U$1-A8.PB5@194
- net HI_A6: now also U$1-A8.PB6@195
- net HI_A7: now also U$1-A8.PB7@196
- net HI_A8: now also U$1-A8.PB8@198
- net HI_A9: now also U$1-A8.PB9@199
- net HI_CLK: now also U$1-A8.PC0@35
- net HI_D0: now also U$1-A8.PK0@126
- net HI_D1: now also U$1-A8.PK1@127
- net HI_D2: now also U$1-A8.PK2@128
- net HI_D3: now also U$1-A8.PK3@186
- net HI_D4: now also U$1-A8.PK4@187
- net HI_D5: now also U$1-A8.PK5@188
- net HI_D6: now also U$1-A8.PK6@189
- net HI_D7: now also U$1-A8.PK7@190
- net HI_R/!W!: now also IC6.2B1, U$1-A8.PC1@36; no longer IC1.A
- net HI_RD4: now also U$1-A8.PC8@140; no longer IC6.2B1
- net HI_RD5: now also U$1-A8.PC9@141; no longer IC6.2B0
- net N$2: no longer XMOS-CTRL.CLK@A12
- net N$4: no longer XMOS-LED.X3D43@C16
- net N$56: no longer XMOS-LED.X3D42@D16
- net N$57: no longer XMOS-LED.X3D41@C17
- net N$63: no longer XMOS-LED.X3D40@D17
- net R/!W!: now also IC6.2A1; no longer IC1.B, XMOS-A8BUS.X2D23@W20
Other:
- note added: "6 Slots"
- note added: "8-bit bus RTS / CTS"
- note added: "Atari Interface / Level Converters for FPGA"
- note added: "Debug / UART"
- note added: "Each SPI covers 2 slots"
- note added: "ICE40, PQFP144 - Decodes a8 bus - Interface to FPGA - SMI interface"
- note added: "Per slot !IRQ!, UART and !SS!"
- note added: "SMI"
- note added: "STM32F7, PQ208 - 32MB x8 SDRAM - 1xSPI per 2 slots - UART, !SS! and !IRQ! per slot - UART to outside via debugger - SPI to FPGA - 8-bit // bus to and from FPGA - Interface to A8 logic"
- note added: "XL or XE (5v)"
- note removed: "Atari Interface / Level Converters"
- note removed: "Clock is 24 MHz (within PLL range)"
- note removed: "Debug / XTAG / Link / UART"
- note removed: "Expansion: bus + link (5w)"
- note removed: "I2C"
- note removed: "Per slot !IRQ!"
- note removed: "Sequence 1v ramp to start 1.2ms after VDDIO rail has already reached 3.3v"
- note removed: "Shared SPI / SS per slot"
- note removed: "Slots"
- note removed: "UART"
- note removed: "Vdd should supply 1.4A LD49300 : fixed, 1vout, 5.5vin, 3A"
- note removed: "W9825G6KH"
- note removed: "XMOS 4-tile CPU - 2-way link to debugger - 5-way link to expansion - I2C / Uart offered - A/D/Flags bus decodes A8 bus - Expansion connector - SPI interface to slots"
- note removed: "miniPBI+ (5v)"
- note removed: "t(Delay) = 1.2ms"
- moved on the sheet: AUDIO, C12, C13, C15, C16, C17, C18, C19, C20, C5, C51, C52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

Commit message: Add the FPGA
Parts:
- added IC2: ICE40HX4K-TQ144, samacsys:ICE40HX4K-TQ144
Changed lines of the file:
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@@
 <setting verticaltext="up"/>
 </settings>
-<grid distance="0.1" unitdist="inch" unit="inch" style="lines" multiple="1" display="yes" altdistance="0.01" altunitdist="inch" altunit="inch"/>
+<grid distance="0.1" unitdist="inch" unit="inch" style="lines" multiple="1" display="no" altdistance="0.01" altunitdist="inch" altunit="inch"/>
 <layers>
 <layer number="1" name="Top" color="4" fill="1" visible="no" active="no"/>
@@
 <part name="SUPPLY2" library="supply2" deviceset="GND" device=""/>
 <part name="U$3" library="sjg-power" deviceset="+1.2V" device=""/>
+<part name="IC2" library="samacsys" deviceset="ICE40HX4K-TQ144" device=""/>
 </parts>
 <sheets>
@@
 <attribute name="VALUE" x="317.5" y="-76.2" size="1.778" layer="96"/>
 </instance>
+<instance part="IC2" gate="G$1" x="391.16" y="99.06" smashed="yes">
+<attribute name="NAME" x="491.49" y="127" size="1.778" layer="95" align="center-left"/>
+<attribute name="VALUE" x="491.49" y="124.46" size="1.778" layer="96" align="center-left"/>
+</instance>
 </instances>

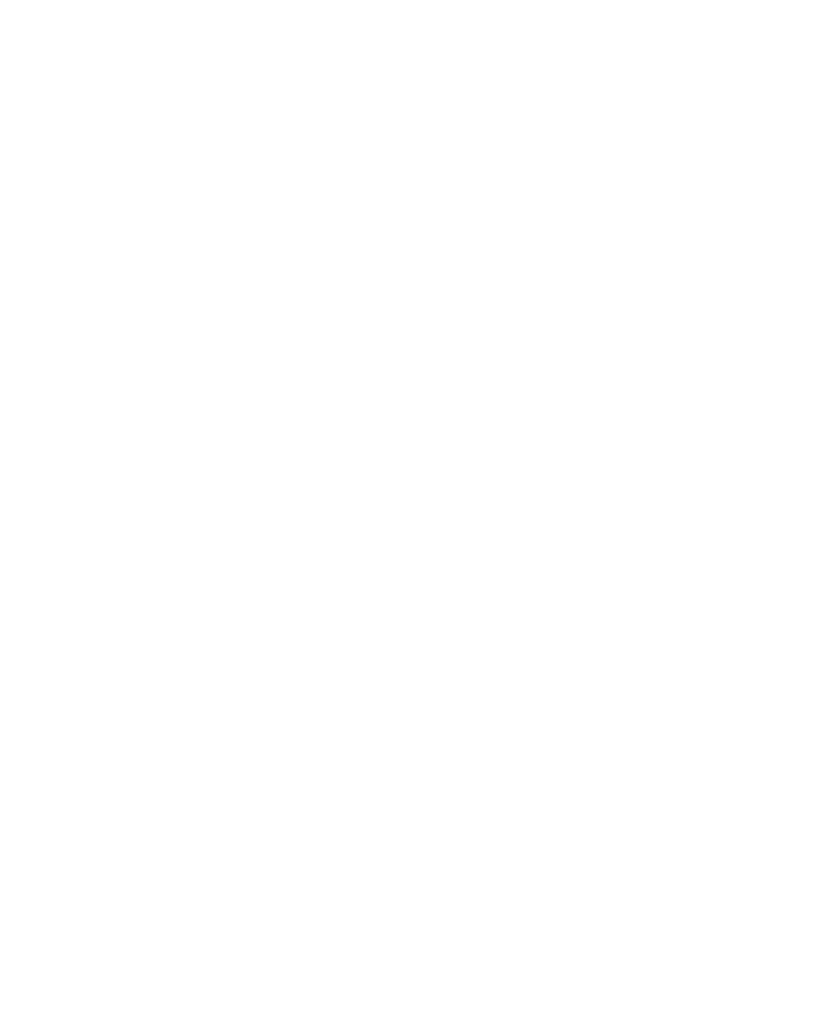
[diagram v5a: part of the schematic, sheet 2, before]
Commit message: Add the DRAM chip. We now have basically all the major parts on the board. Plenty of space :)
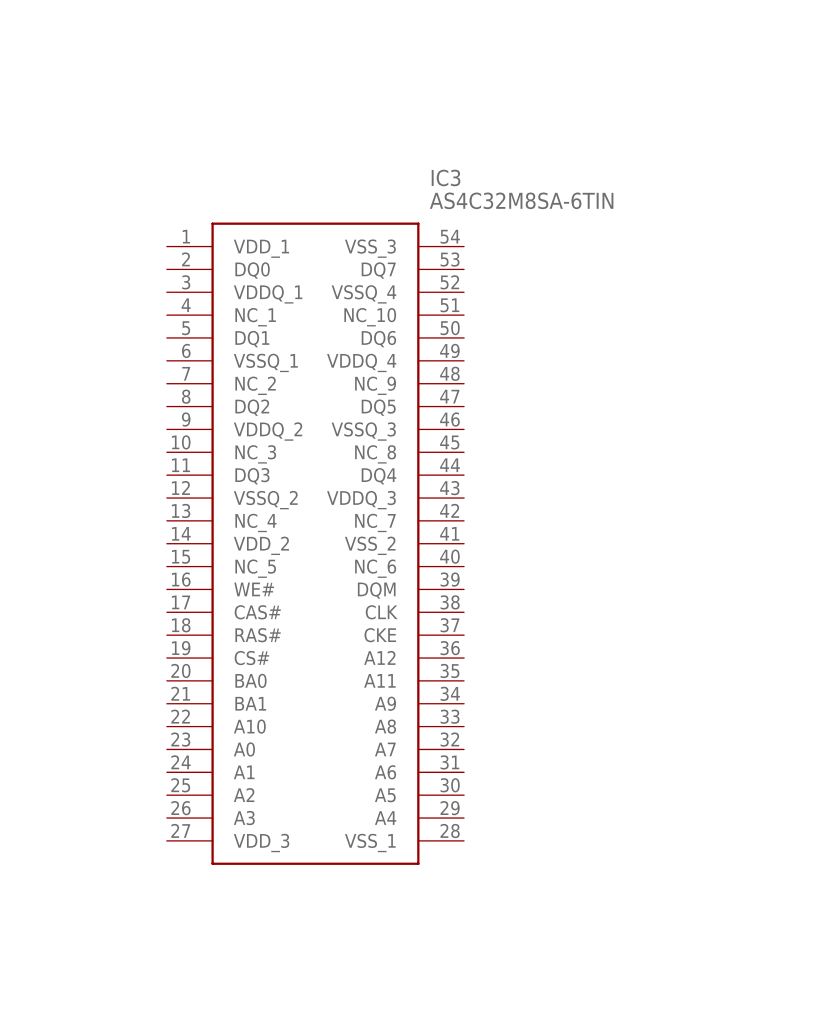
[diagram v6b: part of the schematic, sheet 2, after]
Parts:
- added IC3: AS4C32M8SA-6TIN, samacsys:MT48LC32M8A2P-6AG
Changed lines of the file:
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@@
 <part name="U$3" library="sjg-power" deviceset="+1.2V" device=""/>
 <part name="IC2" library="samacsys" deviceset="ICE40HX4K-TQ144" device=""/>
+<part name="IC3" library="samacsys" deviceset="MT48LC32M8A2P-6AG" device="" value="AS4C32M8SA-6TIN"/>
 </parts>
 <sheets>
@@
 <attribute name="VALUE" x="491.49" y="124.46" size="1.778" layer="96" align="center-left"/>
 </instance>
+<instance part="IC3" gate="G$1" x="398.78" y="-45.72" smashed="yes">
+<attribute name="NAME" x="427.99" y="-38.1" size="1.778" layer="95" align="center-left"/>
+<attribute name="VALUE" x="427.99" y="-40.64" size="1.778" layer="96" align="center-left"/>
+</instance>
 </instances>
